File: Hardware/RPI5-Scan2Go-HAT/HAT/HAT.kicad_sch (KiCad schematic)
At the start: 33 parts, among them J1 RPi_GPIO, J10 Conn_01x02_Socket, J12 Conn_01x02_Socket, J13 Conn_01x02_Socket, J14 Conn_01x02_Socket, J15 Jack-DC 5V, J18 Conn_01x02_Socket, J19 Conn_01x02_Socket, J2 Conn_01x04_Socket, J20 Conn_01x05_Socket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

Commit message: Updated PCB to v0.2.1, improved docs
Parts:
- J15: Farnell (none) -> FCR681466P; Mouser 710-694106301002 -> (none)
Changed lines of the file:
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@@
 	(title_block
 		(title "Scan2Go FDS-HAT")
-		(date "2024-05-14")
-		(rev "V0.2")
+		(date "2024-05-21")
+		(rev "V0.2.1")
 		(company "UMC Utrecht")
 		(comment 1 "Casper R. Tak")
@@
 			)
 		)
-		(property "Datasheet" "https://nl.mouser.com/datasheet/2/445/694106301002-1719831.pdf"
+		(property "Datasheet" "https://nl.farnell.com/cliff-electronic-components/fcr681466p/dc-barrel-conn-jack-2-1mm-2-5mm/dp/2759202"
 			(at 26.67 25.146 0)
 			(effects
@@
 			)
 		)
-		(property "Mouser" "710-694106301002"
+		(property "Mouser" ""
 			(at 25.4 24.13 0)
 			(effects
@@
 			)
 		)
-		(property "Farnell" ""
+		(property "Farnell" "FCR681466P"
 			(at 25.4 24.13 0)
 			(effects

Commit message: Improved bom file and cleanup
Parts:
- D1: value c -> 5.0V
- F1: value 10 A -> 5 A
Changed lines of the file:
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@@
 			)
 		)
-		(property "Value" "10 A"
+		(property "Value" "5 A"
 			(at 48.387 19.685 90)
 			(effects
@@
 			)
 		)
-		(property "Value" "c"
+		(property "Value" "5.0V"
 			(at 46.482 29.21 0)
 			(effects
@@
 				)
 				(hide yes)
+			)
+		)
+		(property "Populate" ""
+			(at 57.15 26.67 0)
+			(effects
+				(font
+					(size 1.27 1.27)
+				)
 			)
 		)
@@
 					(size 1.524 1.524)
 				)
-			)
-		)
+				(hide yes)
+			)
+		)

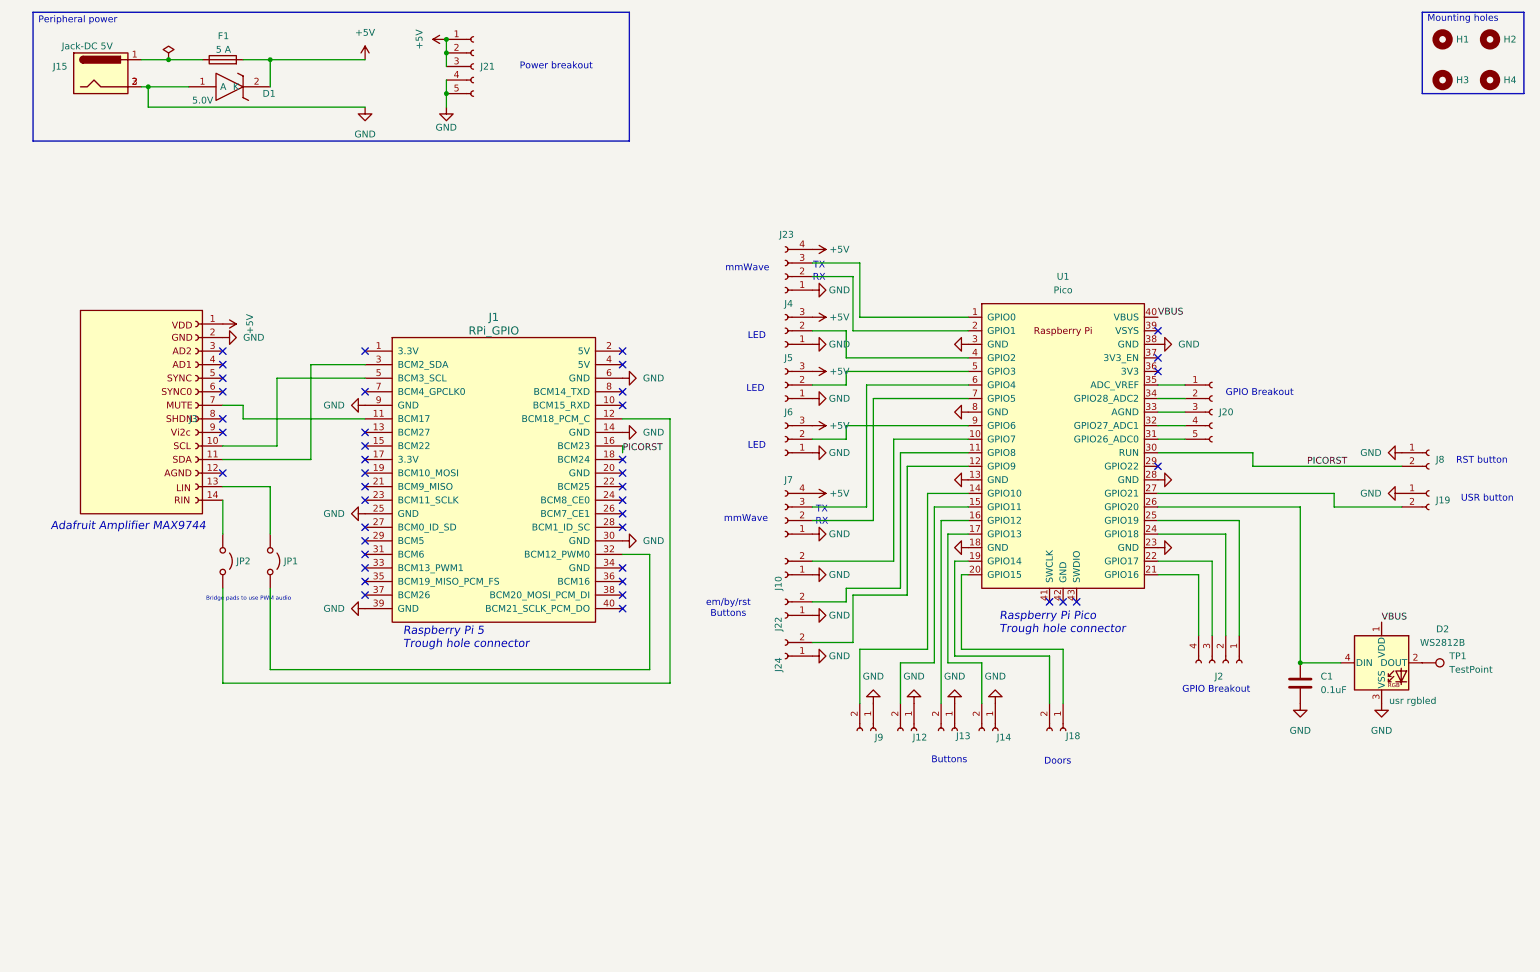
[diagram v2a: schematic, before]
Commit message: added V0.3 of pcb (srlatch) and added librarys
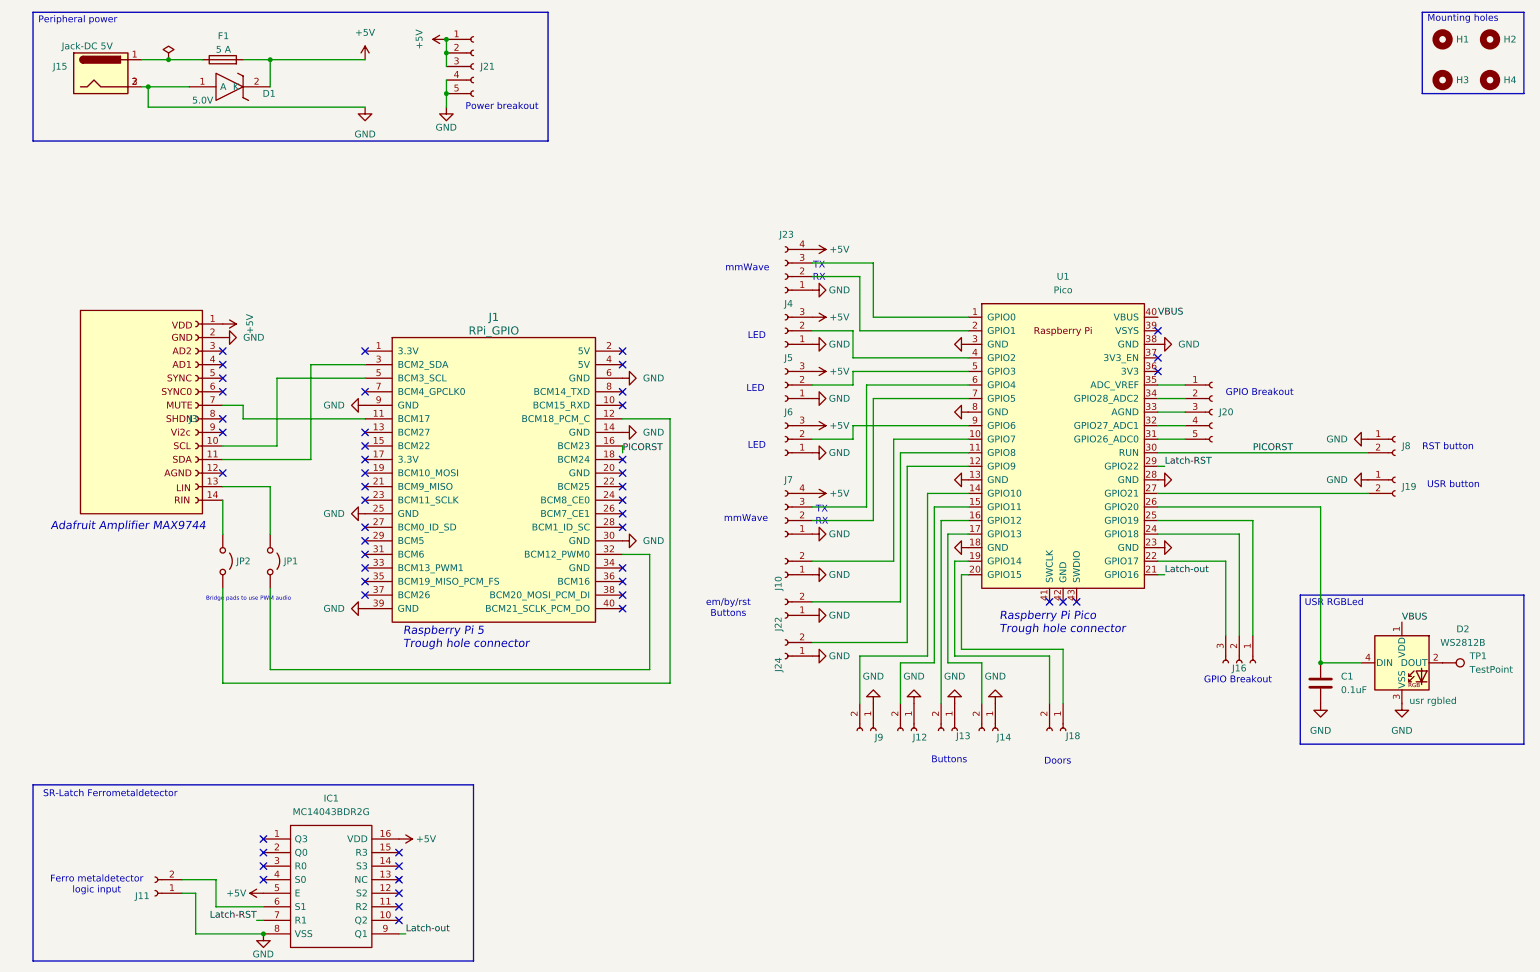
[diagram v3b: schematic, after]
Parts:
- removed J2: Conn_01x04_Socket, Connector_JST:JST_EH_B4B-EH-A_1x04_P2.50mm_Vertical, symbol Connector:Conn_01x04_Socket
- added IC1: MC14043BDR2G, SOIC127P600X175-16N, symbol SamacSys_Parts:MC14043BDR2G
- added J11: Conn_01x02_Socket, Connector_JST:JST_EH_B2B-EH-A_1x02_P2.50mm_Vertical, symbol Connector:Conn_01x02_Socket
- added J16: Conn_01x03_Socket, Connector_JST:JST_EH_B3B-EH-A_1x03_P2.50mm_Vertical, symbol Connector:Conn_01x03_Socket
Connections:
- net +5V: now also IC1.16 (VDD), IC1.5 (E)
- net GND: now also IC1.8 (VSS), J11.1 (Pin_1)
- net at U1.25 (GPIO19): now also J16.1 (Pin_1)
- net at U1.24 (GPIO18): now also J16.2 (Pin_2)
- net at U1.22 (GPIO17): now also J16.3 (Pin_3)
- net Latch-out: now reaches U1.21 (GPIO16)
- net Latch-out: now also IC1.9 (Q1)
- net Latch-RST: now reaches U1.29 (GPIO22)
- net Latch-RST: now also IC1.7 (R1)
- new net: IC1.6 (S1), J11.2 (Pin_2)
- no-connect marks 42 -> 51
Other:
- note added: "Ferro metaldetector logic input"
- note added: "SR-Latch Ferrometaldetector"
- note added: "USR RGBLed"
- moved on the sheet: C1, D2, J19, J8, TP1

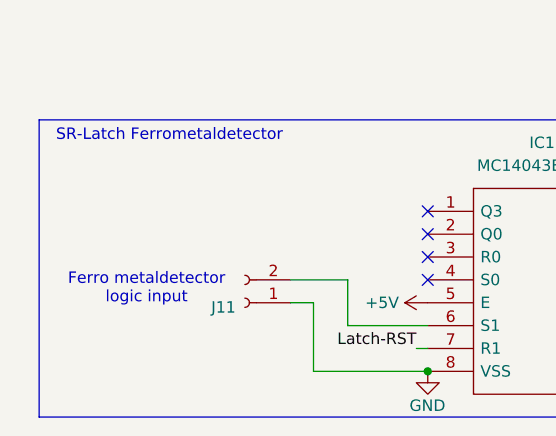
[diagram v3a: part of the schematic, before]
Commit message: rewrote FDS code to set an reset SR-latch and read ferrometal input
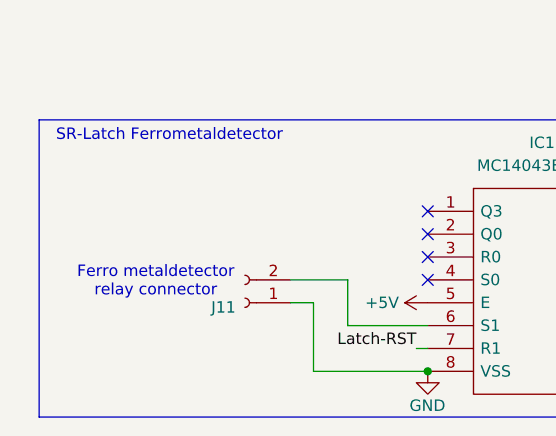
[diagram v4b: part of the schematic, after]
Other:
- note added: "Ferro metaldetector relay connector"
- note removed: "Ferro metaldetector logic input"
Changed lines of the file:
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@@
 		)
 	)
-	(text "Ferro metaldetector \nlogic input\n"
+	(text "Ferro metaldetector \nrelay connector\n\n"
 		(exclude_from_sim no)
-		(at 24.638 176.276 0)
+		(at 25.654 176.53 0)
 		(effects
 			(font

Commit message: added v0.3.1
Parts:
- added R1: 10K, Resistor_SMD:R_1206_3216Metric_Pad1.30x1.75mm_HandSolder, symbol Device:R
- IC1: footprint SOIC127P600X175-16N -> SamacSys_Parts:SOIC127P600X175-16N
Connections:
- net +5V: now also R1.1
- net at IC1.6 (S1), J11.2 (Pin_2): now also R1.2
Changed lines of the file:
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@@
 		(title "Scan2Go FDS-HAT")
 		(date "2024-05-21")
-		(rev "V0.3")
+		(rev "V0.3.1")
 		(company "UMC Utrecht")
 		(comment 1 "Casper R. Tak")
@@
 	)
 	(junction
+		(at 46.99 175.26)
+		(diameter 0)
+		(color 0 0 0 0)
+	)
+	(junction
 		(at 57.15 21.59)
 		(diameter 0)
@@
 			)
 		)
-		(property "Footprint" "SOIC127P600X175-16N"
+		(property "Footprint" "SamacSys_Parts:SOIC127P600X175-16N"
 			(at 77.47 165.1 0)
 			(effects
@@
 	)
 	(symbol
+		(lib_id "power:+5V")
+		(at 46.99 167.64 0)
+		(unit 1)
+		(exclude_from_sim no)
+		(in_bom yes)
+		(on_board yes)
+		(dnp no)
+		(property "Reference" "#PWR026"
+			(at 46.99 171.45 0)
+			(effects
+				(font
+					(size 1.27 1.27)
+				)
+				(hide yes)
+			)
+		)
+		(property "Value" "+5V"
+			(at 46.99 162.56 0)
+			(effects
+				(font
+					(size 1.27 1.27)
+				)
+			)
+		)
+		(property "Footprint" ""
+			(at 46.99 167.64 0)
+			(effects
+				(font
+					(size 1.27 1.27)
+				)
+				(hide yes)
+			)
+		)
+		(property "Datasheet" ""
+			(at 46.99 167.64 0)
+			(effects
+				(font
+					(size 1.27 1.27)
+				)
+				(hide yes)
+			)
+		)
+		(property "Description" "Power symbol creates a global label with name \"+5V\""
+			(at 46.99 167.64 0)
+			(effects
+				(font
+					(size 1.27 1.27)
+				)
+				(hide yes)
+			)
+		)
+		(pin "1"
+		)
+		(instances
+			(project "HAT"
+				(path "/3ab4cced-3a91-405a-aea0-e8513537e898"
+					(reference "#PWR026")
+					(unit 1)
+				)
+			)
+		)
+	)
+	(symbol
 		(lib_id "Mechanical:MountingHole")
 		(at 276.86 25.4 0)
@@
 					(unit 1)
 				)
+			)
+		)
+	)
+	(symbol
+		(lib_id "Device:R")
+		(at 46.99 171.45 0)
+		(unit 1)
+		(exclude_from_sim no)
+		(in_bom yes)
+		(on_board yes)
+		(dnp no)
+		(fields_autoplaced yes)
+		(property "Reference" "R1"
+			(at 49.53 170.1799 0)
+			(effects
+				(font
+					(size 1.27 1.27)
+				)
+				(justify left)
+			)
+		)
+		(property "Value" "10K"
+			(at 49.53 172.7199 0)
+			(effects
+				(font
+					(size 1.27 1.27)
+				)
+				(justify left)
+			)
+		)
+		(property "Footprint" "Resistor_SMD:R_1206_3216Metric_Pad1.30x1.75mm_HandSolder"
+			(at 45.212 171.45 90)
+			(effects
+				(font
+					(size 1.27 1.27)
+				)
+				(hide yes)
+			)
+		)
+		(property "Datasheet" "~"
+			(at 46.99 171.45 0)
+			(effects
+				(font
+					(size 1.27 1.27)
+				)
+				(hide yes)
+			)
+		)
+		(property "Description" "Resistor"
+			(at 46.99 171.45 0)
+			(effects
+				(font
+					(size 1.27 1.27)
+				)
+				(hide yes)
+			)
+		)
+		(property "Populate" ""
+			(at 46.99 171.45 0)
+			(effects
+				(font
+					(size 1.27 1.27)
+				)
+			)
+		)
+		(property "Farnell" "3545485 "
+			(at 46.99 171.45 0)
+			(effects
+				(font
+					(size 1.27 1.27)
+				)
+				(hide yes)
+			)
+		)
+		(pin "1"
+		)
+		(pin "2"
+		)
+		(instances
+			(project "HAT"
+				(path "/3ab4cced-3a91-405a-aea0-e8513537e898"
+					(reference "R1")
+					(unit 1)
+				)

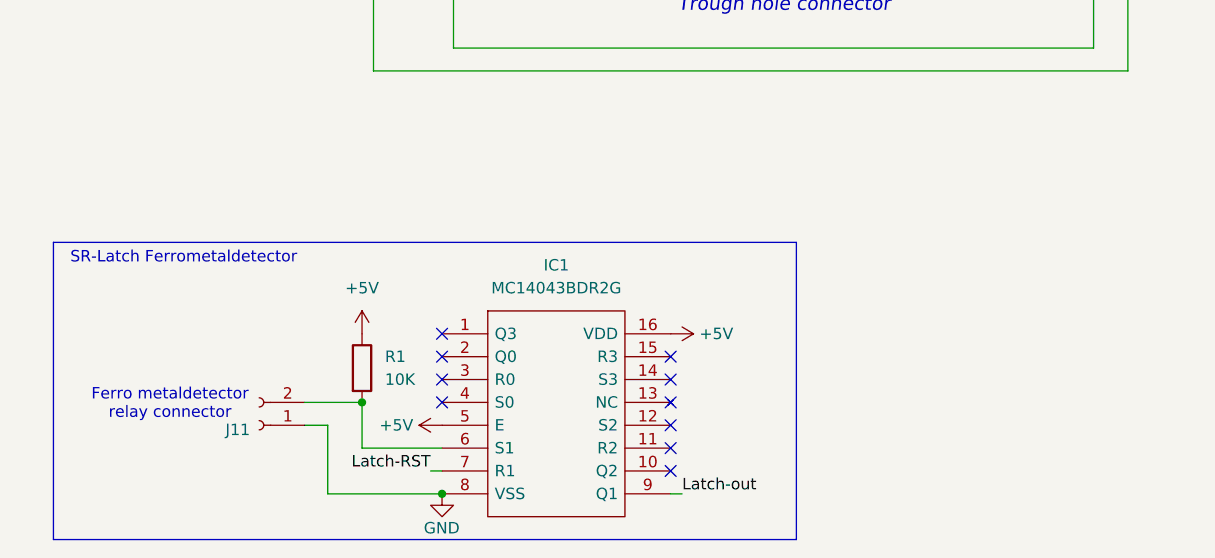
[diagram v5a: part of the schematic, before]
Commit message: updated PCB design to 0.4
- added amplifier trigger to schematic and pcb
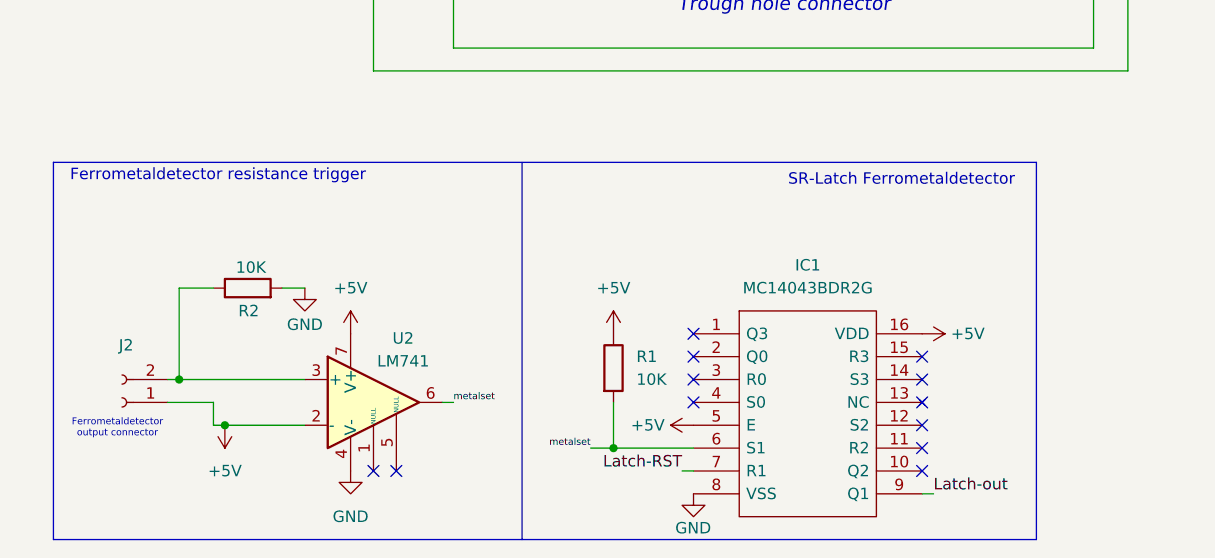
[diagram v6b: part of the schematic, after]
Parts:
- removed J11: Conn_01x02_Socket, Connector_JST:JST_EH_B2B-EH-A_1x02_P2.50mm_Vertical, symbol Connector:Conn_01x02_Socket
- added J2: Conn_01x02_Socket, Connector_JST:JST_EH_B2B-EH-A_1x02_P2.50mm_Vertical, symbol Connector:Conn_01x02_Socket
- added R2: 10K, Resistor_SMD:R_1206_3216Metric_Pad1.30x1.75mm_HandSolder, symbol Device:R
- added U2: LM741, Package_SO:SOIC-8_3.9x4.9mm_P1.27mm, symbol Amplifier_Operational:LM741
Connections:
- net +5V: now also J2.1 (Pin_1), U2.2 (-), U2.7 (V+)
- net GND: now also R2.2, U2.4 (V-)
- net metalset: now reaches IC1.6 (S1), R1.2
- net metalset: now also U2.6
- new net: J2.2 (Pin_2), R2.1, U2.3 (+)
- no-connect marks 51 -> 53
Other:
- note added: "Ferrometaldetector output connector"
- note added: "Ferrometaldetector resistance trigger"
- note removed: "Ferro metaldetector relay connector"
- moved on the sheet: IC1, R1

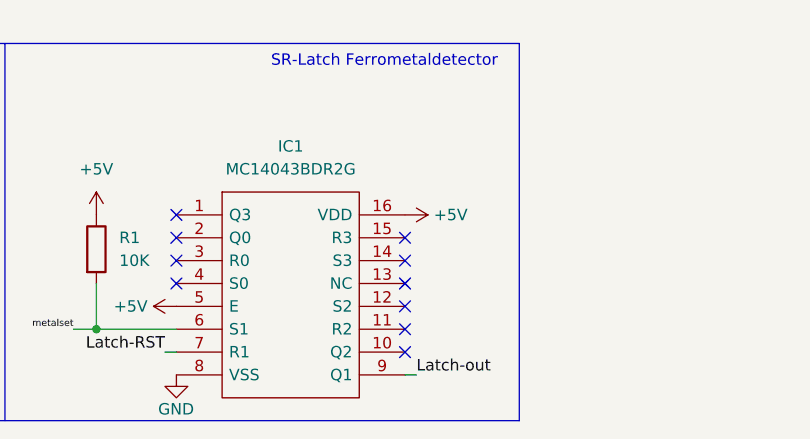
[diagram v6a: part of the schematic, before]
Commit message: bom(s) updated. 3d models added.
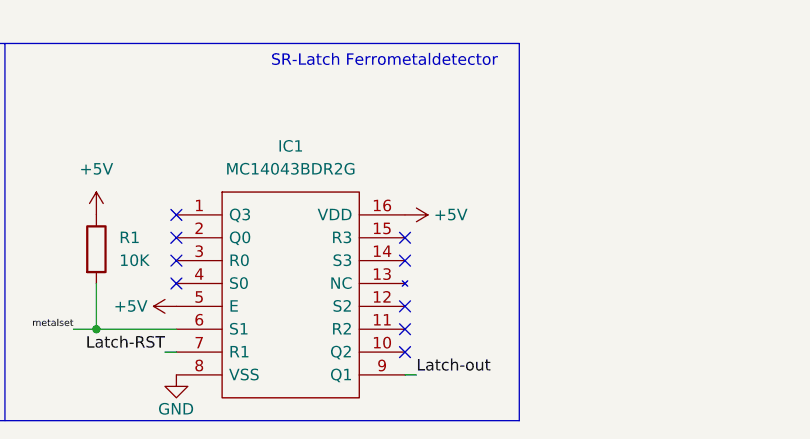
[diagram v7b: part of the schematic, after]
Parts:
- R2: Farnell (none) -> 3545485
- U2: Farnell (none) -> 3117118
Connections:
- no-connect marks 53 -> 52
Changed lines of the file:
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@@
 	)
 	(no_connect
-		(at 109.22 175.26)
-	)
-	(no_connect
 		(at 74.93 111.76)
 	)
@@
 			)
 		)
+		(property "Farnell" "3545485 "
+			(at 34.29 162.56 90)
+			(effects
+				(font
+					(size 1.27 1.27)
+				)
+				(hide yes)
+			)
+		)
 		(pin "1"
 		)
@@
 			(at 48.26 175.26 0)
 			(effects
+				(font
+					(size 1.27 1.27)
+				)
+				(hide yes)
+			)
+		)
+		(property "Populate" ""
+			(at 48.26 175.26 0)
+			(effects
+				(font
+					(size 1.27 1.27)
+				)
+			)
+		)
+		(property "Farnell" "3117118 "
+			(at 48.26 175.26 0)
+			(effects

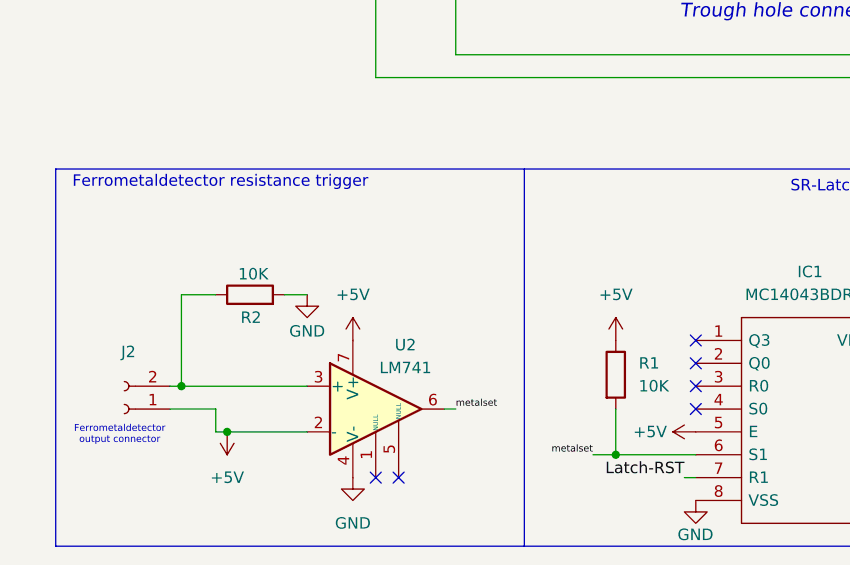
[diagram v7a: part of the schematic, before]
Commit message: made opamp in design optional
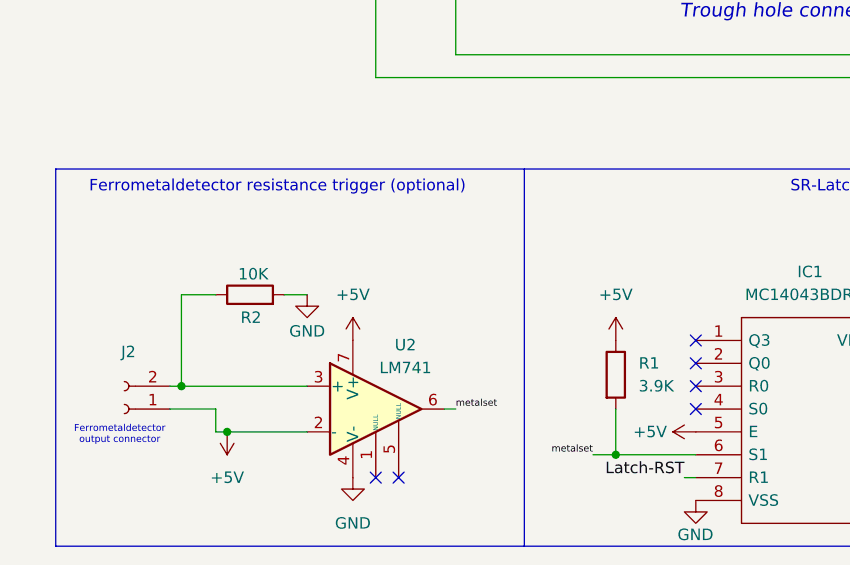
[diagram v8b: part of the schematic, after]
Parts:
- R1: value 10K -> 3.9K; Purpose (none) -> A resistor is required to trigger the latch, matching the v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
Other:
- note added: "Ferrometaldetector resistance trigger (optional)"
- note removed: "Ferrometaldetector resistance trigger"
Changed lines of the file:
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@@
 	(title_block
 		(title "Scan2Go FDS-HAT")
-		(date "2024-06-05")
-		(rev "V0.4")
+		(date "2024-06-10")
+		(rev "V0.4.1")
 		(company "UMC Utrecht")
 		(comment 1 "Casper R. Tak")
@@
 		)
 	)
-	(text "Ferrometaldetector resistance trigger"
+	(text "Ferrometaldetector resistance trigger (optional)"
 		(exclude_from_sim no)
-		(at 30.988 150.114 0)
+		(at 37.338 150.622 0)
 		(effects
 			(font
@@
 			)
 		)
-		(property "Value" "10K"
+		(property "Value" "3.9K"
 			(at 77.47 172.7199 0)
 			(effects
@@
 			(at 74.93 171.45 0)
 			(effects
+				(font
+					(size 1.27 1.27)
+				)
+				(hide yes)
+			)
+		)
+		(property "Purpose" "A resistor is required to trigger the latch, matching the varying outputs of 2.2K and 6.8K from the metal detector."
+			(at 74.93 171.45 0)
+			(effects
